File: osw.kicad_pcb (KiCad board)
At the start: 2 copper layers, 46 x 41.4 mm, 60 parts, among them J1 Conn_01x02, J2 microSD_MEM2067-02-180-00-A_R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, J3 2169890001, Q1 Q_NMOS_ToshibaSMD, SW1 SPST_EVQ-P7J01P, SW2 SPST_EVQ-P7J01P, SW3 SPST_EVQ-P7J01P, SW4 SPST_EVQ-P7J01P, U1 L96-M33, U10 BMA400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

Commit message: Corrected a library FP.  Also corrected the fact the regulators need to be pulled up to work correctly.  Rotated LCD FP so it folds correctly now.  Only thing left is to find the nasty short that is causing me issues.
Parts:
- U11: footprint open-Smartwatch:GC9A01_IPS_display -> open-Smartwatch:GC9A01_IPS_display_under
- moved R7 6.21 mm to (158.4, 106.8)
- moved Q1 6.16 mm to (156.0, 106.6)
- moved C18 5.83 mm to (154.4, 109.2), turned to 0 degrees
- moved R19 2.40 mm to (153.8, 107.6), turned to 90 degrees
- moved U11 0.09 mm to (150.6, 109.5)
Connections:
- U3 pad 14: /~{TFT_RST} -> /PIN_LED
- U3 pad 20: /PIN_LED -> /~{TFT_RST}
- U5 pad 3: unconnected-(U5-EN-Pad3) -> /VCC
- U7 pad 3: unconnected-(U7-EN-Pad3) -> /VCC_SW
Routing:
- net /3V3_2: track 72.5 -> 61.7 mm
- net /MOSI: track 41.1 -> 35.9 mm
- net /SCLK: track 36.4 -> 34.1 mm
- net /PIN_LED: track 10.3 -> 8.56 mm
- net GND: track 23.6 -> 22.1 mm, vias 63 -> 62
- net /LEDK: track 2.88 -> 4.35 mm
- net /VCC: track 9.91 -> 11.1 mm
- net /VCC_SW: track 10.1 -> 11.3 mm
- net /TFT_CS: track 24.5 -> 23.6 mm
- net Net-(U11-LEDA): track 3.67 -> 3.07 mm
- net /SCL: track 34.1 -> 33.5 mm
- net /FLASH: track 41.0 -> 41.5 mm

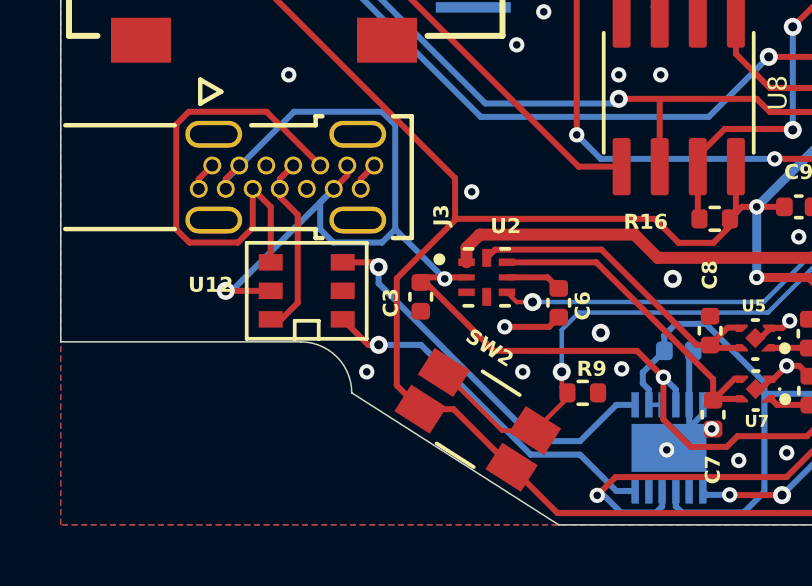
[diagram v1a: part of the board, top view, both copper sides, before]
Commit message: Fixing the ESD diode array that was mis-pinned.
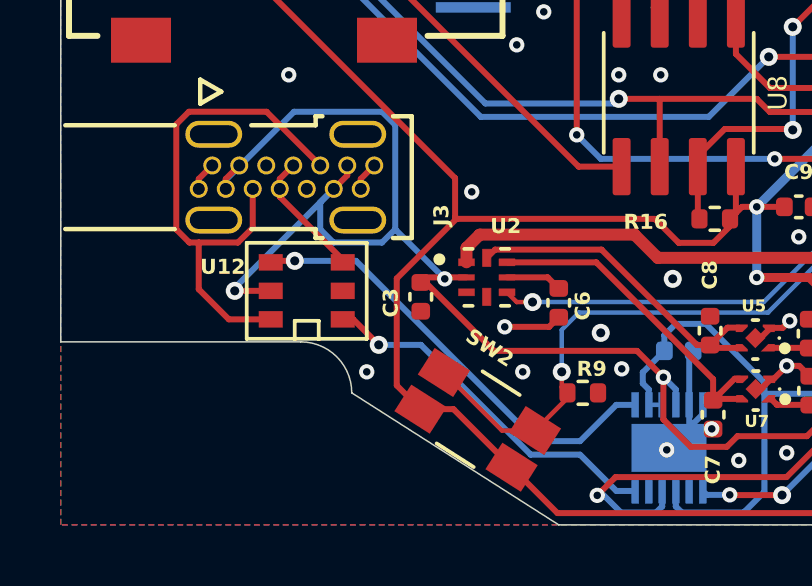
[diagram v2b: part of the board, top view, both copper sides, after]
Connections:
- U12 pad 3: /D- -> /D_ESD+
- U12 pad 4: /D_ESD- -> /D-
- U12 pad 6: /D_ESD+ -> /D_ESD-
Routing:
- net /D-: track 13.0 -> 15.2 mm
- net /D_ESD+: track 6.14 -> 4.29 mm
- net /D_ESD-: track 16.1 -> 17.8 mm
- net /VBUS: track 59.4 -> 58.9 mm
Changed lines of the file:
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@@
     (property "manf#" "IP4234CZ6,125")
     (attr smd)
-    (fp_text reference "U12" (at 3.2 0.2) (layer "F.SilkS")
+    (fp_text reference "U12" (at 2.8 0.8) (layer "F.SilkS")
         (effects (font (size 0.5 0.5) (thickness 0.12) bold))
     )
@@
       (net 1 "GND") (pinfunction "GND") (pintype "bidirectional"))
     (pad "3" smd rect (at -1.2 0.95 270) (size 0.55 0.8) (layers "F.Cu" "F.Paste" "F.Mask")
-      (net 47 "/D-") (pinfunction "I/O2A") (pintype "bidirectional"))
+      (net 18 "/D_ESD+") (pinfunction "I/O1B") (pintype "bidirectional"))
     (pad "4" smd rect (at 1.2 0.95 270) (size 0.55 0.8) (layers "F.Cu" "F.Paste" "F.Mask")
-      (net 19 "/D_ESD-") (pinfunction "I/O2B") (pintype "bidirectional"))
+      (net 47 "/D-") (pinfunction "I/O2A") (pintype "bidirectional"))
     (pad "5" smd rect (at 1.2 0 270) (size 0.55 0.8) (layers "F.Cu" "F.Paste" "F.Mask")
       (net 3 "/VBUS") (pinfunction "VB") (pintype "bidirectional"))
     (pad "6" smd rect (at 1.2 -0.95 270) (size 0.55 0.8) (layers "F.Cu" "F.Paste" "F.Mask")
-      (net 18 "/D_ESD+") (pinfunction "I/O1B") (pintype "bidirectional"))
+      (net 19 "/D_ESD-") (pinfunction "I/O2B") (pintype "bidirectional"))
   )
   (footprint "open-Smartwatch:C_0402_1005Metric_osw" (layer "F.Cu")
@@
   (segment (start 149.75 122.35) (end 149.17 122.35) (width 0.2) (layer "F.Cu") (net 3))
   (segment (start 146.55 118.95) (end 146.1 119.4) (width 0.2) (layer "F.Cu") (net 3))
-  (segment (start 144 122.8) (end 142.5 122.8) (width 0.2) (layer "F.Cu") (net 3))
   (segment (start 157.089 125.6805) (end 156.2085 124.8) (width 0.2) (layer "F.Cu") (net 3))
   (segment (start 149.16 122.52) (end 149 122.52) (width 0.2) (layer "F.Cu") (net 3))
@@
   (segment (start 156.2085 124.8) (end 151.44 124.8) (width 0.2) (layer "F.Cu") (net 3))
   (segment (start 149.8 122.4) (end 149.75 122.35) (width 0.2) (layer "F.Cu") (net 3))
+  (segment (start 144 122.8) (end 142.8 122.8) (width 0.2) (layer "F.Cu") (net 3))
   (segment (start 158 128) (end 159.2 128) (width 0.2) (layer "F.Cu") (net 3))
   (segment (start 150.525 122.35) (end 149.85 122.35) (width 0.2) (layer "F.Cu") (net 3))
   (segment (start 159.555 127.645) (end 161.872396 127.645) (width 0.2) (layer "F.Cu") (net 3))
   (segment (start 142.5 119.07) (end 142.95 118.62) (width 0.2) (layer "F.Cu") (net 3))
-  (via (at 142.5 122.8) (size 0.6) (drill 0.3) (layers "F.Cu" "B.Cu") (net 3))
+  (via (at 142.8 122.8) (size 0.6) (drill 0.3) (layers "F.Cu" "B.Cu") (net 3))
   (via (at 157.089 125.6805) (size 0.51) (drill 0.25) (layers "F.Cu" "B.Cu") (net 3))
   (via (at 170.2 120.85) (size 0.51) (drill 0.25) (layers "F.Cu" "B.Cu") (net 3))
@@
   (via (at 165 120.904207) (size 0.51) (drill 0.25) (layers "F.Cu" "B.Cu") (net 3))
   (segment (start 142.5 119.4) (end 142.5 119.104558) (width 0.2) (layer "B.Cu") (net 3))
-  (segment (start 142.7 122.8) (end 146.1 119.4) (width 0.2) (layer "B.Cu") (net 3))
   (segment (start 157.5 126.6) (end 157.5 126.08513) (width 0.2) (layer "B.Cu") (net 3))
-  (segment (start 142.5 122.8) (end 142.7 122.8) (width 0.2) (layer "B.Cu") (net 3))
   (segment (start 165 120.904207) (end 165.054207 120.85) (width 0.2) (layer "B.Cu") (net 3))
   (segment (start 148.148742 120.747916) (end 147.706658 121.19) (width 0.2) (layer "B.Cu") (net 3))
@@
   (segment (start 147.706658 121.19) (end 146.089784 121.19) (width 0.2) (layer "B.Cu") (net 3))
   (segment (start 144.774558 116.83) (end 147.710216 116.83) (width 0.2) (layer "B.Cu") (net 3))
+  (segment (start 142.8 122.8) (end 142.8 122.7) (width 0.2) (layer "B.Cu") (net 3))
   (segment (start 165.054207 120.85) (end 170.2 120.85) (width 0.2) (layer "B.Cu") (net 3))
   (segment (start 147.710216 116.83) (end 148.148742 117.268526) (width 0.2) (layer "B.Cu") (net 3))
@@
   (segment (start 148.148742 117.268526) (end 148.148742 120.747916) (width 0.2) (layer "B.Cu") (net 3))
   (segment (start 157.5 126.08513) (end 157.09537 125.6805) (width 0.2) (layer "B.Cu") (net 3))
+  (segment (start 142.8 122.7) (end 146.1 119.4) (width 0.2) (layer "B.Cu") (net 3))
   (segment (start 163.212467 121.7) (end 156.9 121.7) (width 0.4) (layer "F.Cu") (net 4))
   (segment (start 177.86 122.6) (end 178.31 122.15) (width 0.4) (layer "F.Cu") (net 4))
@@
   (segment (start 156.890846 111.35) (end 159.487 111.35) (width 0.2) (layer "B.Cu") (net 15))
   (segment (start 156.690846 111.55) (end 156.890846 111.35) (width 0.2) (layer "B.Cu") (net 15))
-  (segment (start 144.3 119.663603) (end 144.9 120.263603) (width 0.2) (layer "F.Cu") (net 18))
-  (segment (start 144.3 119.4) (end 144.3 119.663603) (width 0.2) (layer "F.Cu") (net 18))
-  (segment (start 144.9 120.263603) (end 144.9 123.2) (width 0.2) (layer "F.Cu") (net 18))
-  (segment (start 144.35 123.75) (end 144 123.75) (width 0.2) (layer "F.Cu") (net 18))
-  (segment (start 144.9 123.2) (end 144.35 123.75) (width 0.2) (layer "F.Cu") (net 18))
+  (segment (start 146.4 121.763603) (end 144.3 119.663603) (width 0.2) (layer "F.Cu") (net 18))
+  (segment (start 144.3 119.663603) (end 144.3 119.4) (width 0.2) (layer "F.Cu") (net 18))
+  (segment (start 146.4 121.85) (end 146.4 121.763603) (width 0.2) (layer "F.Cu") (net 18))
   (segment (start 144.3 119.4) (end 144.3 119.07) (width 0.2) (layer "F.Cu") (net 18))
   (segment (start 144.3 119.07) (end 144.75 118.62) (width 0.2) (layer "F.Cu") (net 18))
-  (segment (start 144 120) (end 144 121.85) (width 0.2) (layer "F.Cu") (net 19))
   (segment (start 140.851258 120.751474) (end 140.851258 117.248742) (width 0.2) (layer "F.Cu") (net 19))
-  (segment (start 143.4 119.4) (end 144 120) (width 0.2) (layer "F.Cu") (net 19))
+  (segment (start 142.601471 123.75) (end 141.6 122.748529) (width 0.2) (layer "F.Cu") (net 19))
+  (segment (start 141.6 122.748529) (end 141.6 121.19) (width 0.2) (layer "F.Cu") (net 19))
   (segment (start 140.851258 117.248742) (end 141.27 116.83) (width 0.2) (layer "F.Cu") (net 19))
+  (segment (start 144 123.75) (end 142.601471 123.75) (width 0.2) (layer "F.Cu") (net 19))
   (segment (start 143.4 120.696658) (end 142.906658 121.19) (width 0.2) (layer "F.Cu") (net 19))
-  (segment (start 142.906658 121.19) (end 141.289784 121.19) (width 0.2) (layer "F.Cu") (net 19))
   (segment (start 141.289784 121.19) (end 140.851258 120.751474) (width 0.2) (layer "F.Cu") (net 19))
   (segment (start 143.86 116.83) (end 145.65 118.62) (width 0.2) (layer "F.Cu") (net 19))
   (segment (start 141.27 116.83) (end 143.86 116.83) (width 0.2) (layer "F.Cu") (net 19))
+  (segment (start 142.906658 121.19) (end 141.6 121.19) (width 0.2) (layer "F.Cu") (net 19))
   (segment (start 143.4 119.4) (end 143.4 120.696658) (width 0.2) (layer "F.Cu") (net 19))
+  (segment (start 141.6 121.19) (end 141.289784 121.19) (width 0.2) (layer "F.Cu") (net 19))
   (segment (start 163.1375 107.2375) (end 163.1 107.2) (width 0.2) (layer "F.Cu") (net 21))
   (segment (start 164.9 107.2375) (end 163.1375 107.2375) (width 0.2) (layer "F.Cu") (net 21))
@@
   (segment (start 150.755 107.045) (end 153.755 107.045) (width 0.2) (layer "B.Cu") (net 44))
   (segment (start 153.755 107.045) (end 153.8 107.09) (width 0.2) (layer "B.Cu") (net 44))
-  (segment (start 147.59525 122.00475) (end 147.4405 121.85) (width 0.2) (layer "F.Cu") (net 47))
-  (segment (start 147.4405 121.85) (end 146.4 121.85) (width 0.2) (layer "F.Cu") (net 47))
-  (via (at 147.59525 122.00475) (size 0.6) (drill 0.3) (layers "F.Cu" "B.Cu") (net 47))
-  (segment (start 147.59525 122.554134) (end 152.851116 127.81) (width 0.2) (layer "B.Cu") (net 47))
-  (segment (start 147.59525 122.00475) (end 147.59525 122.554134) (width 0.2) (layer "B.Cu") (net 47))
-  (segment (start 155.519999 126.6) (end 156.15 126.6) (width 0.2) (layer "B.Cu") (net 47))
+  (segment (start 144.05 121.8) (end 144 121.85) (width 0.2) (layer "F.Cu") (net 47))
+  (segment (start 144.8 121.8) (end 144.05 121.8) (width 0.2) (layer "F.Cu") (net 47))
+  (via (at 144.8 121.8) (size 0.6) (drill 0.3) (layers "F.Cu" "B.Cu") (net 47))
+  (segment (start 144.8 121.8) (end 146.841116 121.8) (width 0.2) (layer "B.Cu") (net 47))
   (segment (start 152.851116 127.81) (end 154.309999 127.81) (width 0.2) (layer "B.Cu") (net 47))
+  (segment (start 155.519999 126.6) (end 156.15 126.6) (width 0.2) (layer "B.Cu") (net 47))
+  (segment (start 146.841116 121.8) (end 152.851116 127.81) (width 0.2) (layer "B.Cu") (net 47))
   (segment (start 154.309999 127.81) (end 155.519999 126.6) (width 0.2) (layer "B.Cu") (net 47))
   (segment (start 167.75 117.9375) (end 167.75 119.15) (width 0.15) (layer "F.Cu") (net 49))
@@
   (segment (start 173.6 122.7) (end 170.576089 125.723911) (width 0.2) (layer "B.Cu") (net 56))
   (segment (start 172.6 119.9) (end 173.6 120.9) (width 0.2) (layer "B.Cu") (net 56))
-  (segment (start 147.6 124.6) (end 147.25 124.6) (width 0.2) (layer "F.Cu") (net 58))
-  (segment (start 147.25 124.6) (end 146.4 123.75) (width 0.2) (layer "F.Cu") (net 58))
+  (segment (start 146.75 123.75) (end 147.6 124.6) (width 0.2) (layer "F.Cu") (net 58))
+  (segment (start 146.4 123.75) (end 146.75 123.75) (width 0.2) (layer "F.Cu") (net 58))
   (via (at 147.6 124.6) (size 0.6) (drill 0.3) (layers "F.Cu" "B.Cu") (net 58))
   (segment (start 149.004719 124.6) (end 152.664719 128.26) (width 0.2) (layer "B.Cu") (net 58))

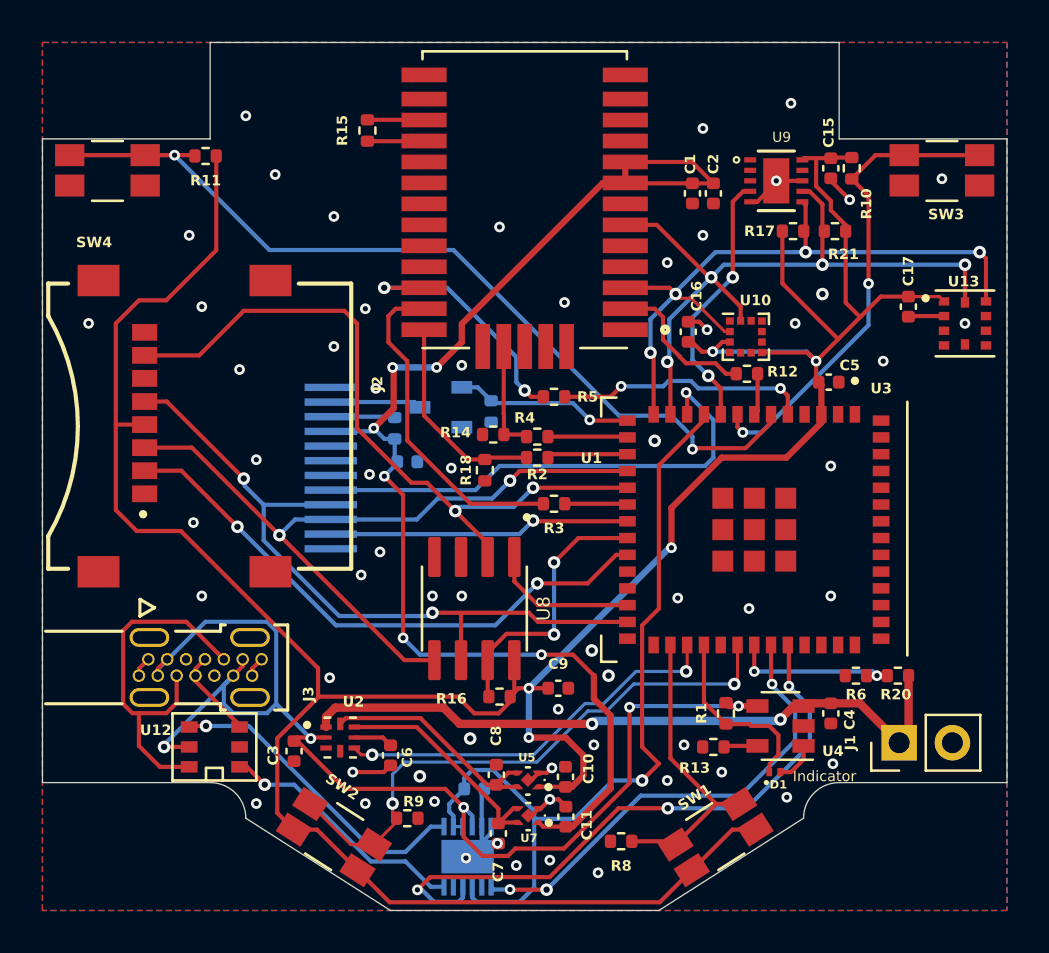
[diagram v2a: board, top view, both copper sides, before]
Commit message: Updates to a bunch of symbols and the entire schematic now matches the libs....  Now onto fixing the short.
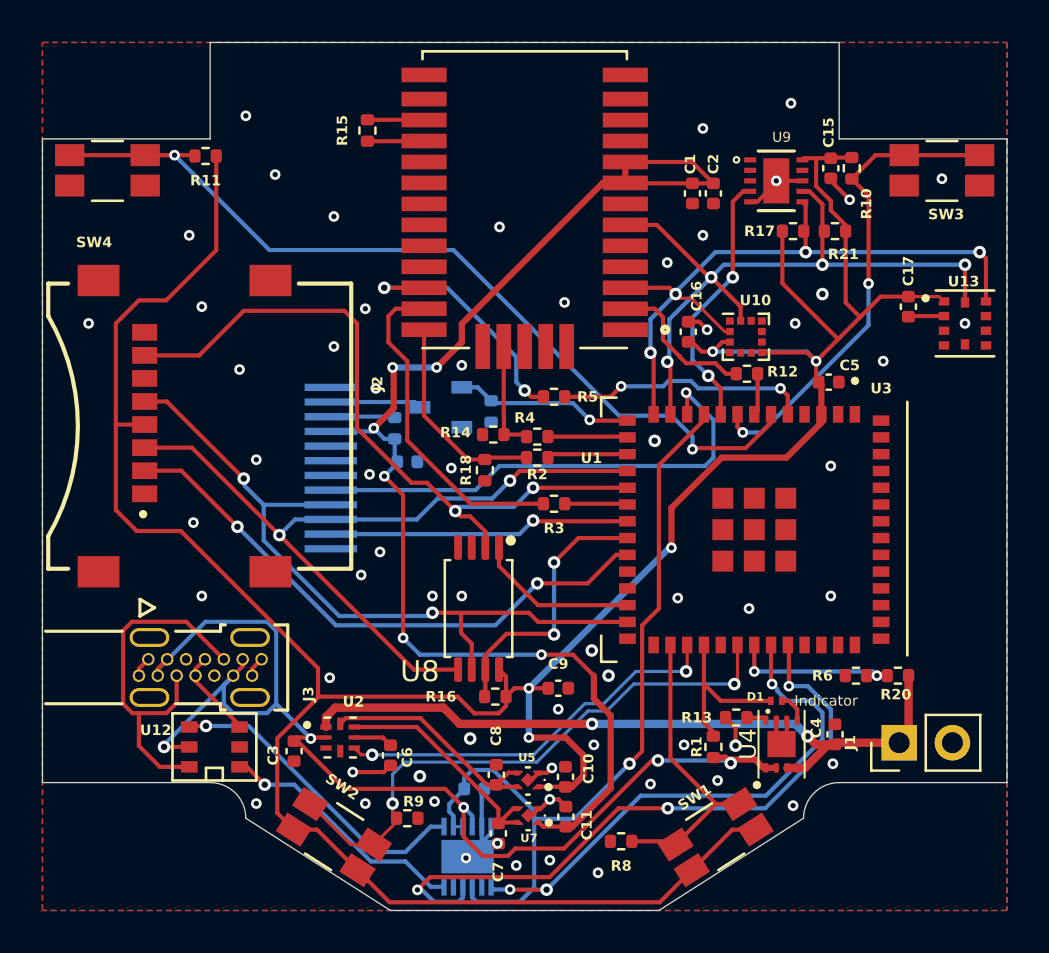
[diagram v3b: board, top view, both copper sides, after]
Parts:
- U4: value MCP73831T-2ACI_OT -> MCP73831T-2ACI; footprint open-Smartwatch:SOT-23-5 -> Allard_dfn_qfn:PSON9P50_200X300X80L40X25T135X125L
- U8: footprint open-Smartwatch:SOIC127P600X175-8N_microchipRAM -> AllardSOP:SOP8P65_300X640X120L47X24N
- moved D1 3.40 mm to (172.0, 120.6)
- moved R13 1.77 mm to (170.1, 121.4)
- moved R1 1.71 mm to (169.0, 122.8), turned to -90 degrees
- moved C4 1.02 mm to (174.8, 122.2), turned to 90 degrees
- moved U4 0.87 mm to (172.2, 122.7), turned to 0 degrees
- moved R16 0.20 mm to (158.6, 120.4)
- moved U8 0.20 mm to (157.8, 116.2), turned to 180 degrees
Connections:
- C8 pad 2: GND -> unconnected-(C8-Pad2)
- U4 pad 1: Net-(D1-K) -> /VBUS
- U4 pad 2: GND -> /VBUS
- U4 pad 4: /VBUS -> /VBAT
- U4 pad 5: Net-(U4-PROG) -> Net-(D1-K)
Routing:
- net GND: track 22.1 -> 26.1 mm, vias 62 -> 63
- net /RX: track 22.5 -> 25.0 mm
- net /VBAT: track 32.9 -> 34.9 mm
- net /VBUS: track 58.9 -> 57.0 mm
- net /TX: track 29.9 -> 31.8 mm
- net /v3p3USB: track 40.2 -> 38.7 mm
- net /MOSI: track 35.9 -> 37.2 mm
- net /STAT_PWR: track 8.87 -> 7.86 mm
- net /RAM_CS: track 7.03 -> 7.78 mm
- net /SCLK: track 34.1 -> 34.8 mm
- net Net-(U4-PROG): track 1.61 -> 0.95 mm
- net Net-(D1-K): track 2.01 -> 1.43 mm

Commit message: Updating some FPs.
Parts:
- C1, C17, C18: value cap0402_1p0u10V -> 1u; footprint open-Smartwatch:C_0402_1005Metric_osw -> AllardChip:CAPC100X50X60L25N
- C12, C15, C16, C2, C5, C6, C7, C8, C9: value cap0402_p1u10V -> 100n; footprint open-Smartwatch:C_0402_1005Metric_osw -> AllardChip:CAPC100X50X55L25N
- R10, R11, R13, R16, R17, R20, R21, R4, R6, R7, R8, R9: value res0402_10k -> 10k; footprint open-Smartwatch:R_0402_1005Metric_osw -> AllardChip:RESC100X50X40L25N
- R12, R2, R3, R5: value res0402_1k -> 1k; footprint open-Smartwatch:R_0402_1005Metric_osw -> AllardChip:RESC100X50X40L25N
- moved R10 0.20 mm to (175.8, 95.2)
- moved R12 0.20 mm to (170.6, 105.2)
- moved R13 0.20 mm to (170.1, 121.2)
- moved R2 0.20 mm to (160.6, 109.2)
- moved R9 0.20 mm to (154.4, 126.0)
- moved C2 0.20 mm to (169.2, 96.4)
- moved R16 0.20 mm to (158.6, 120.6)
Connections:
- C8 pad 2: unconnected-(C8-Pad2) -> GND
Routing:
- net GND: track 26.1 -> 26.6 mm

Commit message: Updates.
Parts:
- U8: footprint AllardSOP:SOP8P65_300X640X120L47X24N -> AllardSOP:SOP8P65_300X640X120L47X24L

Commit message: Moving things to kicad 8.
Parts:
- U8: value 23K256-I/SN -> 23K256T-I/ST
- moved C5 0.40 mm to (174.5, 105.0)
- moved R20 0.40 mm to (177.8, 119.8)
- moved R6 0.40 mm to (175.8, 119.8)
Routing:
- net /v3p3USB: track 38.7 -> 39.2 mm

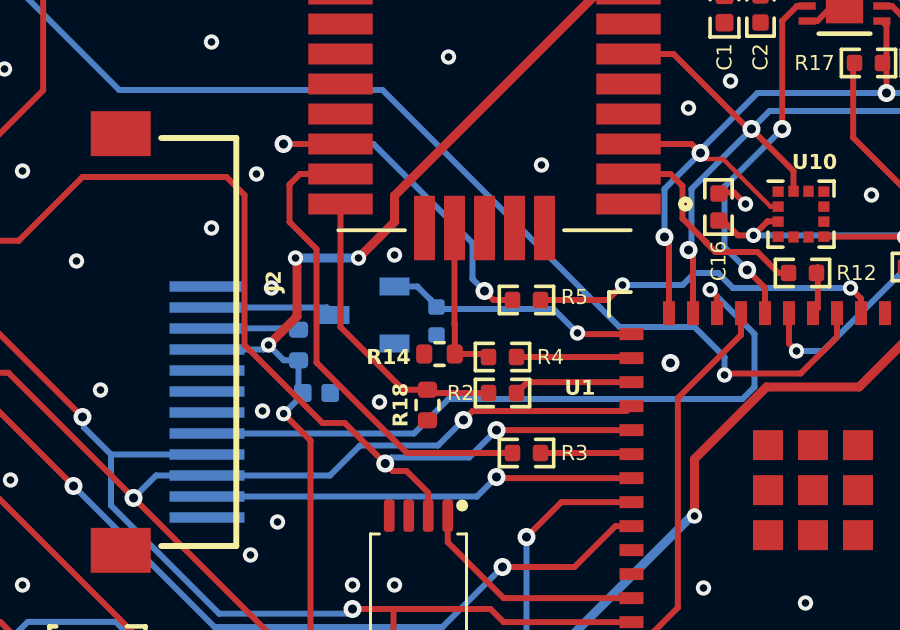
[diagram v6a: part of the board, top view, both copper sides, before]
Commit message: Updating the FP for a SOT23.
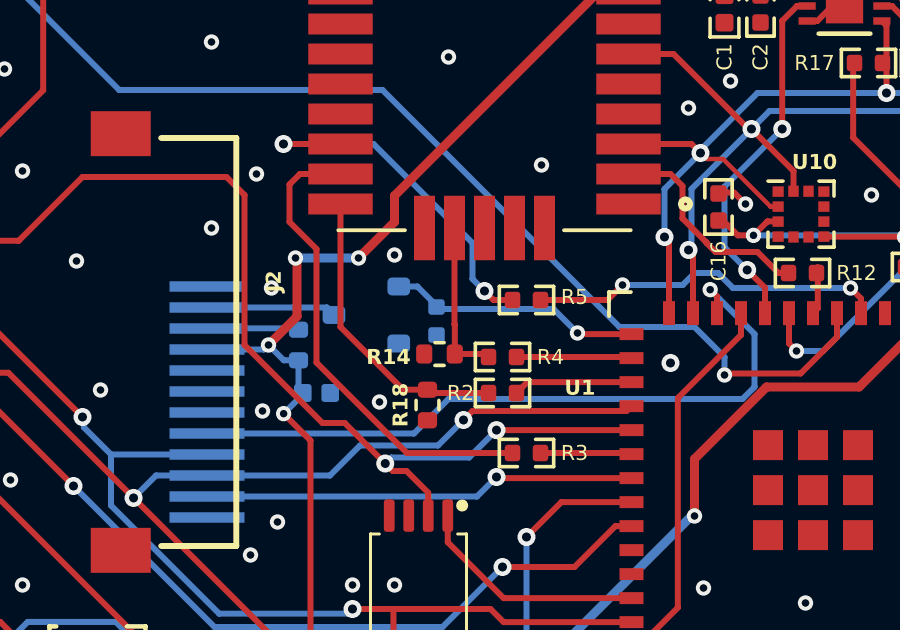
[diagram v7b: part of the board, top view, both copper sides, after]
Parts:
- Q1: footprint open-Smartwatch:SOT95P247X115-3N -> AllardSOT:SOT23-3P95_240X105L35X42L
- moved Q1 0.06 mm to (156.1, 106.6), turned to -90 degrees
